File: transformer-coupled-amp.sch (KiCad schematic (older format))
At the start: 9 parts

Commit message: Annotate schematics
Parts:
- added C10, C12: 10u x 25V, symbol Device:CP
- added C11, C13: 500u x 25V, symbol Device:CP
- added C2, C9: 200u x 25V, symbol Device:CP
- added C3: 10u, symbol Device:CP
- added C4: 0.01u, symbol Device:C
- added C5, C8: 0.033u, symbol Device:C
- added C6: 0.3u, symbol Device:C
- added D1: Д9В, symbol Device:D
- added D2: Д9Д, symbol Device:D
- added LS1: 4..16Ω, symbol Device:Speaker
- added Q1, Q2: МП25Б, Package_TO_SOT_THT:TO-11-3, symbol Device:Q_PNP_BEC
- added Q4: МП41А, Package_TO_SOT_THT:TO-11-3, symbol Device:Q_PNP_BEC
- added Q5: МП40A, Package_TO_SOT_THT:TO-11-3, symbol Device:Q_PNP_BEC
- added Q6, Q7: П213Б, Package_TO_SOT_THT:TO-11-3, symbol Device:Q_PNP_BEC
- added R1: 15K, symbol Device:R
- added R10: 910, symbol Device:R
- added R11: 200, symbol Device:R
- added R12: 3K, symbol Device:R
- added R13, R16: 6.8K*, symbol Device:R
- added R14: 350, symbol Device:R
- added R15: 51*, symbol Device:R
- added R17: 330, symbol Device:R
- added R4: 9.1K, symbol Device:R
- added R5: 510K, symbol Device:R
- added R6: 6.2K, symbol Device:R
- added R8: 1K, symbol Device:R
- added RV1, RV2: 47K, symbol Device:R_POT
- added T1: Transformer_1P_1S, symbol Device:Transformer_1P_1S
- added МП37А: Q?, symbol Device:Q_NPN_BEC
- added МП37А111: Q_NPN_BEC, symbol Device:Q_NPN_BEC
- C1: renamed from C?; value CP -> 100u x 25V
- C7: renamed from C?; value CP -> 10u
- R2: renamed from R?; value 150 -> 270K
- RV3: renamed from RV?; value R_POT -> 47K
- gave numbers to parts that had none: 5
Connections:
- net GND: now also J1.2, R9.2, RV3.3, C13.1, C8.2, C9.1, Q7.2 (E), R10.2, R11.2, R12.2, R16.2, R17.2, T1.3 (SA), МП37А111.3 (C)
- net at Q3.3 (C), R3.2: now also C3.2
- net at C1.2, R2.1, R3.1: now also R1.2
- new net: C3.1, R8.1, RV2.2
- new net: C5.2, R6.2, RV1.1
- new net: C5.1, C6.1, R8.2, RV1.2
- new net: C6.2, R10.1, RV1.3
- new net: C4.1, Q4.1 (B), R5.2, R6.1
- new net: C4.2, RV2.1
- new net: C8.1, RV2.3
- new net: C10.1, C12.1, T1.4 (SB)
- new net: Q1.1 (B), Q4.3 (C), R4.2, R5.1
- new net: Q4.2 (E), R11.1
- new net: C10.2, D2.1 (K), Q5.1 (B), R13.2
- new net: D1.1 (K), Q1.2 (E), Q2.1 (B)
- new net: C12.2, R15.2, R16.1, МП37А.1 (B)
- new net: D1.2 (A), R12.1, МП37А111.1 (B)
- new net: D2.2 (A), R15.1
- new net: Q5.2 (E), Q6.1 (B), R14.1
- new net: LS1.1, Q6.2 (E), Q7.3 (C), R14.2, МП37А.2 (E)
- new net: Q7.1 (B), R17.1, МП37А.3 (C)
- new net: C11.1, C13.2, LS1.2
- new net -24V: C11.2, C2.2, Q1.3 (C), Q2.3 (C), Q5.3 (C), Q6.3 (C), R1.1, R13.1, R4.1
- new net PREAMP_OUT: Q2.2 (E), T1.1 (AA), МП37А111.2 (E)
- new net PREAMP_OUT_GND: C2.1, C9.2, T1.2 (AB)

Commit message: Finish drawing schematics
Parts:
- removed МП37А: Q?, symbol Device:Q_NPN_BEC
- removed МП37А111: Q_NPN_BEC, symbol Device:Q_NPN_BEC
- added Q5, Q7: МП37А, symbol Device:Q_NPN_BEC
- renumbered C12 to C11, C11 to C12, C7 to C2, C5 to C4, C6 to C5, C4 to C6, C8 to C7, C2 to C8, Q3 to Q1, Q4 to Q2, Q1 to Q3, Q2 to Q4, Q5 to Q6, Q6 to Q8, Q7 to Q9, R7 to R1, R4 to R10, R15 to R14, R16 to R15, R14 to R16, R9 to R4, R1 to R5, R10 to R7, R5 to R9, RV3 to RV1, RV1 to RV2, RV2 to RV3
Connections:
- net GND: now also Q5.3 (C)
- net at C11.2, R14.2, R15.1: now also Q7.1 (B)
- net at D1.2 (A), R12.1: now also Q5.1 (B)
- net at LS1.1, Q8.2 (E), Q9.3 (C)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: now also Q7.2 (E)
- net at Q9.1 (B), R17.1: now also Q7.3 (C)
- net PREAMP_OUT: no longer names the net of Q4.2 (E), T1.1 (AA)
- net PREAMP_OUT: now also Q5.2 (E)
- net PREAMP_OUT_GND: no longer names the net of C8.1, C9.2, T1.2 (AB)
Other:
- note added: "Предусилитель"
- note added: "Темброблок"
- note added: "Усилитель мощности"
- moved on the sheet: C1, C10, C11, C12, C13, C2, C3, C4, C5, C6, C7, C8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

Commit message: Assign footprints
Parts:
- C1: footprint (none) -> Capacitor_THT:CP_Radial_D6.3mm_P2.50mm
- C10, C11, C2, C3: footprint (none) -> Capacitor_THT:CP_Radial_D5.0mm_P2.00mm
- C12, C13: footprint (none) -> Capacitor_THT:CP_Radial_D10.0mm_P5.00mm
- C4, C7: footprint (none) -> Capacitor_THT:C_Disc_D10.0mm_W2.5mm_P5.00mm
- C5: footprint (none) -> Capacitor_THT:C_Rect_L18.0mm_W8.0mm_P15.00mm_FKS3_FKP3
- C6: footprint (none) -> Capacitor_THT:C_Rect_L13.0mm_W5.0mm_P10.00mm_FKS3_FKP3_MKS4
- C8, C9: footprint (none) -> Capacitor_THT:CP_Radial_D8.0mm_P3.50mm
- D1, D2: footprint (none) -> Diode_THT:D_DO-15_P15.24mm_Horizontal
- J1: footprint (none) -> Connector_PinHeader_2.54mm:PinHeader_1x03_P2.54mm_Vertical
- LS1: footprint (none) -> Connector_PinHeader_2.54mm:PinHeader_1x02_P2.54mm_Vertical
- Q1, Q2, Q3, Q4, Q6: footprint Package_TO_SOT_THT:TO-11-3 -> Package_TO_SOT_THT:TO-5-3
- Q5, Q7: footprint (none) -> Package_TO_SOT_THT:TO-5-3
- Q8, Q9: footprint Package_TO_SOT_THT:TO-11-3 -> Package_TO_SOT_THT:TO-3
- R1, R10, R11, R12, R2, R3, R4, R5, R6, R7, R8, R9: footprint (none) -> Resistor_THT:R_Axial_DIN0207_L6.3mm_D2.5mm_P10.16mm_Horizontal
- R13, R14, R15, R16, R17: footprint (none) -> Resistor_THT:R_Axial_DIN0309_L9.0mm_D3.2mm_P15.24mm_Horizontal
- RV1, RV2, RV3: footprint (none) -> Potentiometer_THT:Potentiometer_Bourns_3386C_Horizontal
- T1: footprint (none) -> Transformer_THT:Transformer_Breve_TEZ-44x52

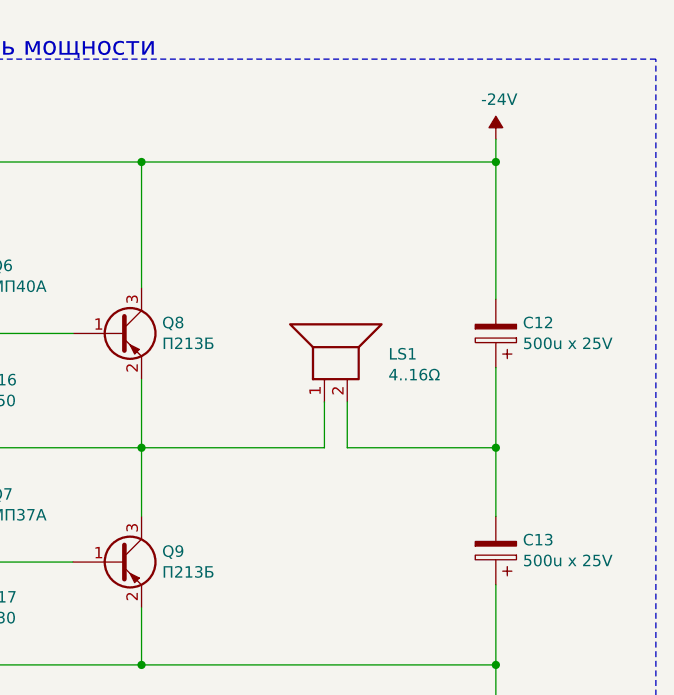
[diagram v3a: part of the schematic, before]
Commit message: Start tracing pcb
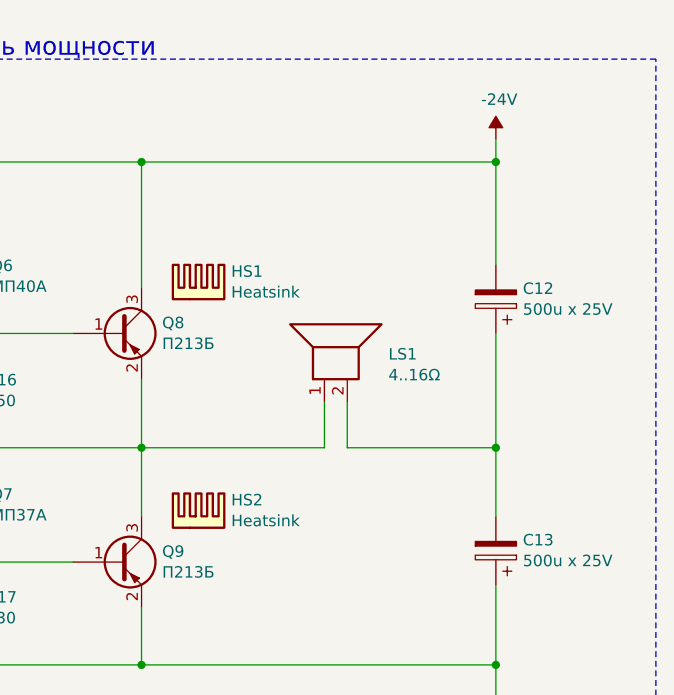
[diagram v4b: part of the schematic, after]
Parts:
- added HS1, HS2: Heatsink, Heatsink:Heatsink_62x40mm_2xFixation3mm, symbol Mechanical:Heatsink
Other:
- moved on the sheet: C12
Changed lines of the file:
@@
 	14800 2600 14150 2600
 Wire Wire Line
-	14800 2250 14800 2600
+	14800 2100 14800 2600
 $Comp
 L Device:CP C13
@@
 Connection ~ 13250 1350
 Wire Wire Line
-	14800 1350 14800 1950
+	14800 1350 14800 1800
 $Comp
 L Device:CP C12
 U 1 1 60915EDC
-P 14800 2100
-F 0 "C12" H 14682 2054 50  0000 R CNN
-F 1 "500u x 25V" H 14682 2145 50  0000 R CNN
-F 2 "Capacitor_THT:CP_Radial_D10.0mm_P5.00mm" H 14838 1950 50  0001 C CNN
-F 3 "https://www.chipdip.by/product0/9000565916" H 14800 2100 50  0001 C CNN
-	1    14800 2100
+P 14800 1950
+F 0 "C12" H 14682 1904 50  0000 R CNN
+F 1 "500u x 25V" H 14682 1995 50  0000 R CNN
+F 2 "Capacitor_THT:CP_Radial_D10.0mm_P5.00mm" H 14838 1800 50  0001 C CNN
+F 3 "https://www.chipdip.by/product0/9000565916" H 14800 1950 50  0001 C CNN
+	1    14800 1950
 	-1   0    0    1
 $EndComp
@@
 Wire Wire Line
 	8000 1150 8000 1250
+$Comp
+L Mechanical:Heatsink HS1
+U 1 1 608E04E9
+P 13500 1950
+F 0 "HS1" H 13642 2071 50  0000 L CNN
+F 1 "Heatsink" H 13642 1980 50  0000 L CNN
+F 2 "Heatsink:Heatsink_62x40mm_2xFixation3mm" H 13512 1950 50  0001 C CNN
+F 3 "~" H 13512 1950 50  0001 C CNN
+	1    13500 1950
+	1    0    0    -1
+$EndComp
+$Comp
+L Mechanical:Heatsink HS2
+U 1 1 608E06E7
+P 13500 2950
+F 0 "HS2" H 13642 3071 50  0000 L CNN
+F 1 "Heatsink" H 13642 2980 50  0000 L CNN
+F 2 "Heatsink:Heatsink_62x40mm_2xFixation3mm" H 13512 2950 50  0001 C CNN
+F 3 "~" H 13512 2950 50  0001 C CNN
+	1    13500 2950
+	1    0    0    -1
+$EndComp
 $EndSCHEMATC

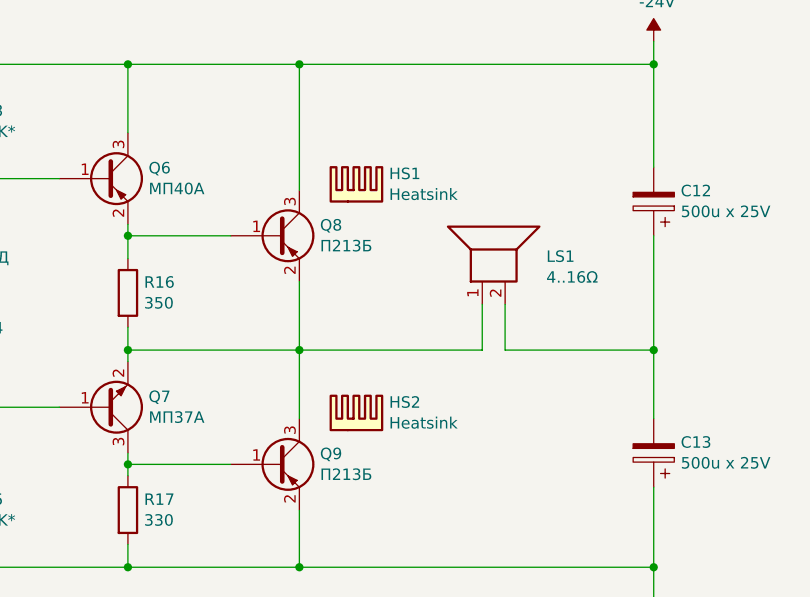
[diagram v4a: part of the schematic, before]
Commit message: Add transformer footrpint
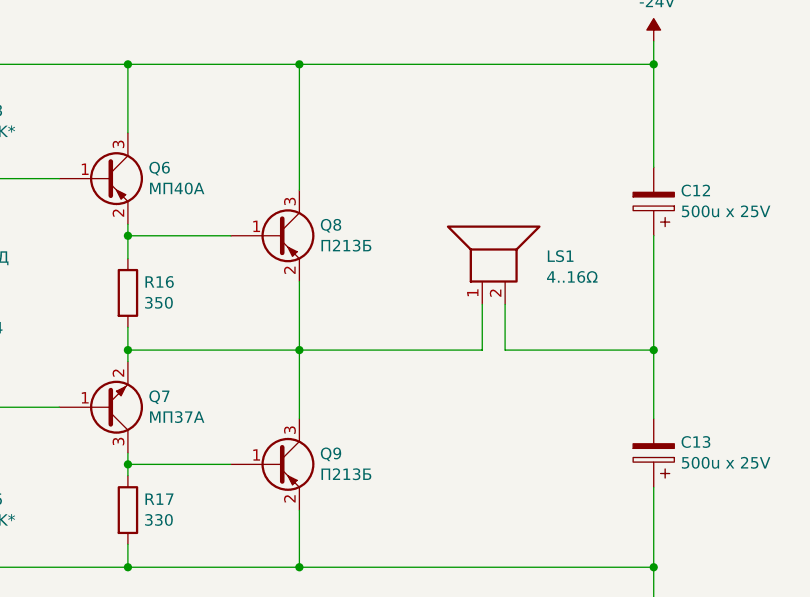
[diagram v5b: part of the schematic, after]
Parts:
- removed HS1, HS2: Heatsink, Heatsink:Heatsink_62x40mm_2xFixation3mm, symbol Mechanical:Heatsink
- Q8, Q9: footprint Package_TO_SOT_THT:TO-3 -> Connector_PinHeader_2.54mm:PinHeader_1x03_P2.54mm_Vertical
- T1: footprint Transformer_THT:Transformer_Breve_TEZ-44x52 -> footprints:Transformer_44x40
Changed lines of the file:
@@
 F 0 "Q8" H 13340 2146 50  0000 L CNN
 F 1 "П213Б" H 13340 2055 50  0000 L CNN
-F 2 "Package_TO_SOT_THT:TO-3" H 13350 2200 50  0001 C CNN
+F 2 "Connector_PinHeader_2.54mm:PinHeader_1x03_P2.54mm_Vertical" H 13350 2200 50  0001 C CNN
 F 3 "~" H 13150 2100 50  0001 C CNN
 	1    13150 2100
@@
 F 0 "Q9" H 13340 3146 50  0000 L CNN
 F 1 "П213Б" H 13340 3055 50  0000 L CNN
-F 2 "Package_TO_SOT_THT:TO-3" H 13350 3200 50  0001 C CNN
+F 2 "Connector_PinHeader_2.54mm:PinHeader_1x03_P2.54mm_Vertical" H 13350 3200 50  0001 C CNN
 F 3 "~" H 13150 3100 50  0001 C CNN
 	1    13150 3100
@@
 F 0 "T1" H 10100 3081 50  0000 C CNN
 F 1 "Transformer_1P_1S" H 10100 2990 50  0000 C CNN
-F 2 "Transformer_THT:Transformer_Breve_TEZ-44x52" H 10100 2700 50  0001 C CNN
+F 2 "footprints:Transformer_44x40" H 10100 2700 50  0001 C CNN
 F 3 "~" H 10100 2700 50  0001 C CNN
 	1    10100 2700
@@
 Wire Wire Line
 	8000 1150 8000 1250
-$Comp
-L Mechanical:Heatsink HS1
-U 1 1 608E04E9
-P 13500 1950
-F 0 "HS1" H 13642 2071 50  0000 L CNN
-F 1 "Heatsink" H 13642 1980 50  0000 L CNN
-F 2 "Heatsink:Heatsink_62x40mm_2xFixation3mm" H 13512 1950 50  0001 C CNN
-F 3 "~" H 13512 1950 50  0001 C CNN
-	1    13500 1950
-	1    0    0    -1
-$EndComp
-$Comp
-L Mechanical:Heatsink HS2
-U 1 1 608E06E7
-P 13500 2950
-F 0 "HS2" H 13642 3071 50  0000 L CNN
-F 1 "Heatsink" H 13642 2980 50  0000 L CNN
-F 2 "Heatsink:Heatsink_62x40mm_2xFixation3mm" H 13512 2950 50  0001 C CNN
-F 3 "~" H 13512 2950 50  0001 C CNN
-	1    13500 2950
-	1    0    0    -1
-$EndComp
 $EndSCHEMATC

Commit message: Finish pcb routing
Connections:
- net GND: no longer C1.1, C13.1, C7.2, C9.1, J1.2, Q5.3 (C), Q9.2 (E), R11.2, R12.2, R15.2, R17.2, R4.2, R7.2, RV1.3, T1.3 (SA)
- new net GND1: C1.1, C7.2, C9.1, J1.2, Q5.3 (C), R11.2, R12.2, R4.2, R7.2, RV1.3
- new net GND2: C13.1, Q9.2 (E), R15.2, R17.2, T1.3 (SA)
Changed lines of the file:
@@
 Wire Wire Line
 	2250 1500 2250 1650
-$Comp
-L power:GND #PWR01
-U 1 1 6087BC2B
-P 1400 1550
-F 0 "#PWR01" H 1400 1300 50  0001 C CNN
-F 1 "GND" H 1405 1377 50  0000 C CNN
-F 2 "" H 1400 1550 50  0001 C CNN
-F 3 "" H 1400 1550 50  0001 C CNN
-	1    1400 1550
-	1    0    0    -1
-$EndComp
 Wire Wire Line
 	1650 1500 1400 1500
-Wire Wire Line
-	1400 1500 1400 1550
 Wire Wire Line
 	2250 3150 2250 2950
@@
 Wire Wire Line
 	8350 2750 8350 2950
-$Comp
-L power:GND #PWR03
-U 1 1 60880D83
-P 9050 3950
-F 0 "#PWR03" H 9050 3700 50  0001 C CNN
-F 1 "GND" H 9055 3777 50  0000 C CNN
-F 2 "" H 9050 3950 50  0001 C CNN
-F 3 "" H 9050 3950 50  0001 C CNN
-	1    9050 3950
-	1    0    0    -1
-$EndComp
 Wire Wire Line
 	9050 3750 9050 3950
@@
 $EndComp
 Connection ~ 14800 3550
-Wire Wire Line
-	14800 3550 14800 3700
-$Comp
-L power:GND #PWR05
-U 1 1 60937C06
-P 14800 3700
-F 0 "#PWR05" H 14800 3450 50  0001 C CNN
-F 1 "GND" H 14805 3527 50  0000 C CNN
-F 2 "" H 14800 3700 50  0001 C CNN
-F 3 "" H 14800 3700 50  0001 C CNN
-	1    14800 3700
-	1    0    0    -1
-$EndComp
 Connection ~ 13250 3550
 Wire Wire Line
@@
 Wire Wire Line
 	8000 1150 8000 1250
+$Comp
+L power:GND1 #PWR0103
+U 1 1 60ABB7B5
+P 9050 3950
+F 0 "#PWR0103" H 9050 3700 50  0001 C CNN
+F 1 "GND1" H 9055 3777 50  0000 C CNN
+F 2 "" H 9050 3950 50  0001 C CNN
+F 3 "" H 9050 3950 50  0001 C CNN
+	1    9050 3950
+	1    0    0    -1
+$EndComp
+$Comp
+L power:GND2 #PWR0104
+U 1 1 60ABC0CC
+P 14800 3800
+F 0 "#PWR0104" H 14800 3550 50  0001 C CNN
+F 1 "GND2" H 14805 3627 50  0000 C CNN
+F 2 "" H 14800 3800 50  0001 C CNN
+F 3 "" H 14800 3800 50  0001 C CNN
+	1    14800 3800
+	1    0    0    -1
+$EndComp
+Wire Wire Line
+	14800 3550 14800 3800
+$Comp
+L power:GND1 #PWR?
+U 1 1 60AC8347
+P 1400 1650
+F 0 "#PWR?" H 1400 1400 50  0001 C CNN
+F 1 "GND1" H 1405 1477 50  0000 C CNN
+F 2 "" H 1400 1650 50  0001 C CNN
+F 3 "" H 1400 1650 50  0001 C CNN
+	1    1400 1650
+	1    0    0    -1
+$EndComp
+Wire Wire Line
+	1400 1500 1400 1650
 $EndSCHEMATC
